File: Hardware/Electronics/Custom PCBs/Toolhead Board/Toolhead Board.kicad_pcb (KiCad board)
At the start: 4 copper layers, 75 x 75 mm, 155 parts, among them J1 USB C Receptacle, J2 Conn_02x04_Odd_Even, J3 Conn_02x08_Odd_Even, J4 Conn_02x08_Odd_Even, J5 Conn_02x08_Odd_Even, J6 Conn_02x04_Odd_Even, J7 Conn_01x02, J8 Conn_01x02, J9 Conn_01x02, Q1 MMBT4403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

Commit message: Update layout
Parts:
- R49, R50, R51: moved to B.Cu
- moved C52 49.8 mm to (80.8, 81.2), turned to 30 degrees
- moved RV1 49.8 mm to (73.0, 81.9), turned to 30 degrees
- moved R53 49.8 mm to (76.7, 82.0), turned to 30 degrees
- moved R48 9.63 mm to (82.9, 43.5), turned to 76 degrees
- moved R49 9.56 mm to (82.9, 43.5), turned to -104 degrees
- moved R44 6.82 mm to (87.7, 45.1), turned to 67 degrees
- moved R52 6.82 mm to (87.7, 45.1), turned to -113 degrees
- moved R51 2.08 mm to (86.1, 44.5), turned to -110 degrees
- moved R47 1.75 mm to (84.5, 43.9), turned to 73 degrees
- moved R45 0.95 mm to (86.1, 44.5), turned to 70 degrees
- moved R50 0.37 mm to (84.5, 43.9), turned to -107 degrees
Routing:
- net 24V_PWM0: track 0.00 -> 23.9 mm, vias 0 -> 2
- net Net-(U11-G1): track 0.00 -> 17.8 mm, vias 0 -> 2
- net Net-(U12-G2): track 0.00 -> 10.9 mm, vias 0 -> 2
- net Net-(U11-G2): track 0.00 -> 9.11 mm, vias 0 -> 2
- net Net-(U13-LED0): track 9.16 -> 15.6 mm
- net Net-(U13-LED3): track 14.3 -> 20.5 mm, vias 0 -> 2
- net Net-(U12-G1): track 4.69 -> 10.7 mm, vias 0 -> 2
- net Net-(U13-LED2): track 25.1 -> 19.5 mm, vias 0 -> 1
- net Net-(U13-LED1): track 19.7 -> 17.2 mm, vias 0 -> 1
- net GND: vias 16 -> 3
- removed copper zone on In1.Cu, net GND
- removed copper zone on In2.Cu, net GND

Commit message: updated pcb
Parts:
- moved C53 47.7 mm to (78.3, 80.2), turned to 90 degrees
- moved R54 44.4 mm to (80.2, 80.1), turned to -90 degrees
- moved RV2 42.1 mm to (81.8, 80.1), turned to 90 degrees
- moved C52 4.88 mm to (76.0, 80.2), turned to 90 degrees
- moved R53 3.14 mm to (74.2, 80.1), turned to -90 degrees
- moved RV1 1.87 mm to (72.7, 80.1), turned to 90 degrees
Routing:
- net MOT_UART: track 11.2 -> 40.1 mm
- net THERM0: track 0.00 -> 18.5 mm
- net THERM1: track 0.00 -> 17.1 mm
- net MOT_DIR: track 7.39 -> 19.0 mm
- net MOT_STP: track 8.75 -> 19.8 mm

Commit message: updated PCB layout
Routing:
- net V_MOT: track 74.8 -> 96.2 mm
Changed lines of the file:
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@@
 		(tags "resistor handsolder")
 		(property "Reference" "RV2"
-			(at -0.05 1.65 270)
+			(at -0.05 1.65 -90)
 			(layer "F.SilkS")
 			(effects
@@
 		)
 		(property "Value" "CG0603MLC-3.3LE"
-			(at 0 1.43 270)
+			(at 0 1.43 -90)
 			(layer "F.Fab")
 			(effects
@@
 		)
 		(fp_text user "${REFERENCE}"
-			(at 0 0 270)
+			(at 0 0 -90)
 			(layer "F.Fab")
 			(effects
@@
 		(tags "capacitor handsolder")
 		(property "Reference" "C53"
-			(at -3.35 0 270)
+			(at -3.35 0 -90)
 			(layer "F.SilkS")
 			(effects
@@
 		)
 		(property "Value" "10u"
-			(at 0 1.68 270)
+			(at 0 1.68 -90)
 			(layer "F.Fab")
 			(effects
@@
 		)
 		(fp_text user "${REFERENCE}"
-			(at 0 0 270)
+			(at 0 0 -90)
 			(layer "F.Fab")
 			(effects
@@
 	)
 	(segment
+		(start 76.000739 60.56667)
+		(end 68.5 68.067409)
+		(width 1.5)
+		(layer "In1.Cu")
+		(net 1)
+	)
+	(segment
 		(start 57.0203 48)
 		(end 57.75 48)
@@
 	)
 	(segment
+		(start 68.5 73.73)
+		(end 68.5 76.27)
+		(width 1.5)
+		(layer "In1.Cu")
+		(net 1)
+	)
+	(segment
 		(start 77.270739 58.366965)
 		(end 75.071033 57.096965)
@@
 	)
 	(segment
+		(start 68.5 68.067409)
+		(end 68.5 71.19)
+		(width 1.5)
+		(layer "In1.Cu")
+		(net 1)
+	)
+	(segment
 		(start 64.28834 59.29667)
 		(end 73.801034 59.29667)
@@
 		(width 1.5)
 		(layer "In1.Cu")
+		(net 1)
+	)
+	(segment
+		(start 68.5 71.19)
+		(end 68.5 73.73)
+		(width 1.5)
+		(layer "In1.Cu")
+		(net 1)
+	)
+	(segment
+		(start 68.5 76.27)
+		(end 68.5 78.81)
+		(width 1.5)
+		(layer "In1.Cu")

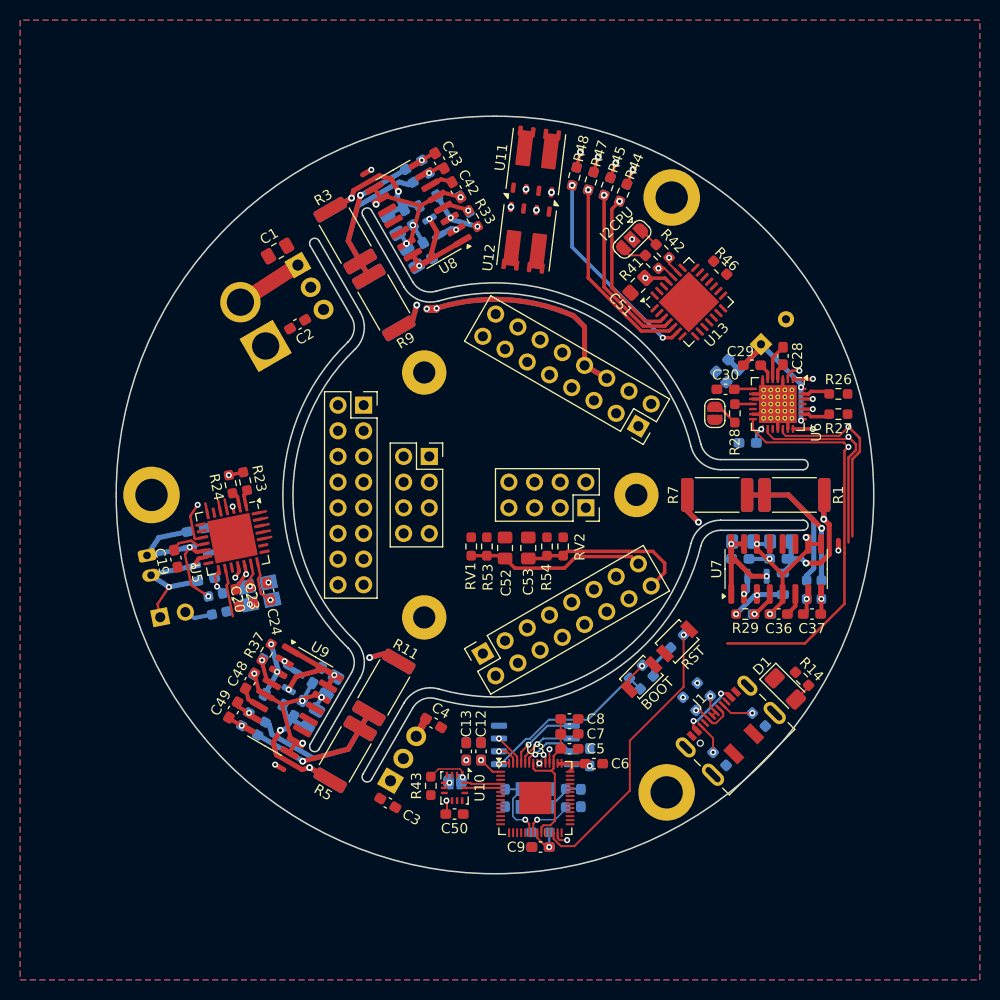
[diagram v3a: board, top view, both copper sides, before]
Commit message: Fix DRC Problems
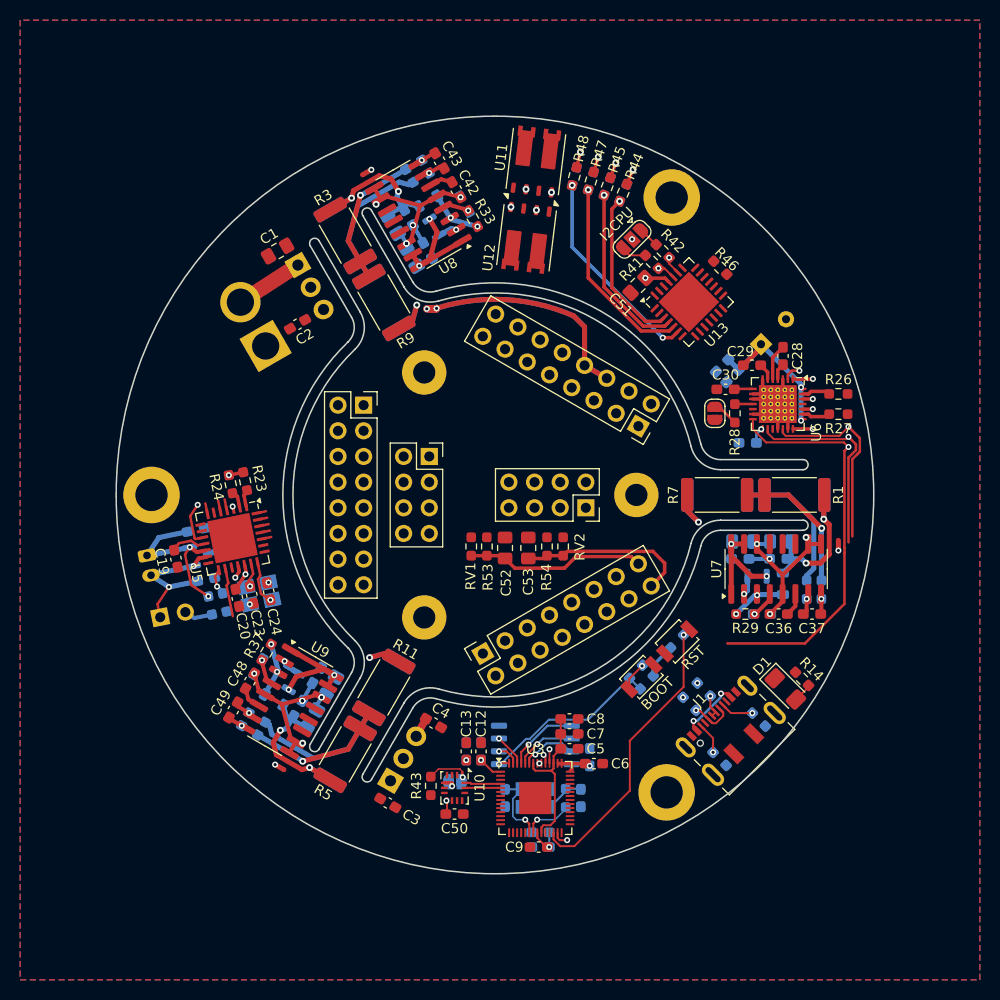
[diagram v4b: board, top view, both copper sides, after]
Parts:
- moved C9 0.18 mm to (79.3, 109.9)
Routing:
- net +3.3V: track 63.7 -> 64.3 mm

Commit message: Update Layout
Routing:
- net 24V_PWM2: track 0.00 -> 55.3 mm, vias 0 -> 2
- net 24V_PWM3: track 0.00 -> 50.3 mm, vias 0 -> 2
- net 24V_PWM1: track 0.00 -> 47.0 mm, vias 0 -> 2
- net 24V_PWM0: track 23.9 -> 68.9 mm, vias 2 -> 4
- net /Microcontroller/LED: track 0.00 -> 39.8 mm
- net MOT_UART: track 40.1 -> 68.1 mm, vias 1 -> 3
- net GND: track 9.27 -> 17.4 mm, vias 3 -> 5
- net +5V: track 5.21 -> 9.34 mm
- net V_MOT: track 96.2 -> 99.0 mm
- net SCK: track 0.94 -> 2.40 mm, vias 0 -> 1
- net MOSI: track 0.94 -> 2.00 mm, vias 0 -> 1

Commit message: Update layout
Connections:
- J3 pad 10: SERVO3 -> D20
- J3 pad 11: SERVO2 -> D21
- J3 pad 12: SERVO4 -> D24
- J3 pad 15: CAN_H -> CAN_L
- J3 pad 16: CAN_L -> CAN_H
- J3 pad 9: SERVO1 -> D1
- J4 pad 1: SERVO5 -> SERVO1
- J4 pad 3: SERVO6 -> SERVO2
- J5 pad 1: D24 -> D25
- J5 pad 13: ADC0 -> +3.3V
- J5 pad 14: ADC1 -> GND
- J5 pad 2: D20 -> ADC0
- J5 pad 3: D25 -> ADC1
- J5 pad 4: D21 -> SERVO4
- J5 pad 5: D1 -> SERVO3
- J5 pad 6: GND -> SERVO6
- J5 pad 7: +5V -> SERVO5
- J5 pad 9: +3.3V -> +5V
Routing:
- net +5V: track 9.34 -> 32.2 mm
- net D20: track 0.00 -> 18.8 mm
- net CAN_H: track 14.4 -> 33.2 mm
- net CAN_L: track 17.1 -> 35.2 mm
- net D1: track 0.00 -> 16.8 mm
- net D24: track 0.00 -> 16.3 mm
- net D21: track 0.00 -> 14.1 mm
- net SDA: track 5.42 -> 19.4 mm
- net SCL: track 5.38 -> 16.8 mm
- net STRAIN_SCK: track 0.00 -> 7.79 mm, vias 0 -> 3
- net STRAIN1_E-: track 74.2 -> 70.1 mm
- net STRAIN3_E-: track 74.2 -> 70.2 mm
- net STRAIN2_E-: track 74.2 -> 70.2 mm
- net STRAIN1_DO: track 0.00 -> 3.95 mm, vias 0 -> 1
- net STRAIN3_DO: track 0.00 -> 3.95 mm, vias 0 -> 1
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
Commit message: Updated PCB
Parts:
- moved R46 1.33 mm to (97.0, 51.2), turned to -135 degrees
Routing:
- net SERVO2: track 0.00 -> 47.5 mm, vias 0 -> 1
- net SERVO1: track 0.00 -> 43.0 mm
- net THERM0: track 18.5 -> 34.1 mm, vias 0 -> 1
- net ADC1: track 0.00 -> 15.5 mm, vias 0 -> 1
- net THERM1: track 17.1 -> 32.1 mm, vias 0 -> 1
- net Net-(U13-~{OE}): track 0.00 -> 1.59 mm
